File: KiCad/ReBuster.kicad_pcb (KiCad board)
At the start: 4 copper layers, 38 x 38 mm, 37 parts, among them U1 10M02SCU169, U2 LM1117-3.3, U3 SN74CBTD16210, U4 SN74LVC16T245DGVR, U5 SN74CBTD16210, U6 SN74CBTD16210, U7 74LVC2T45DC, U8 PLCC_84_plug, U9 PLCC_84_plug

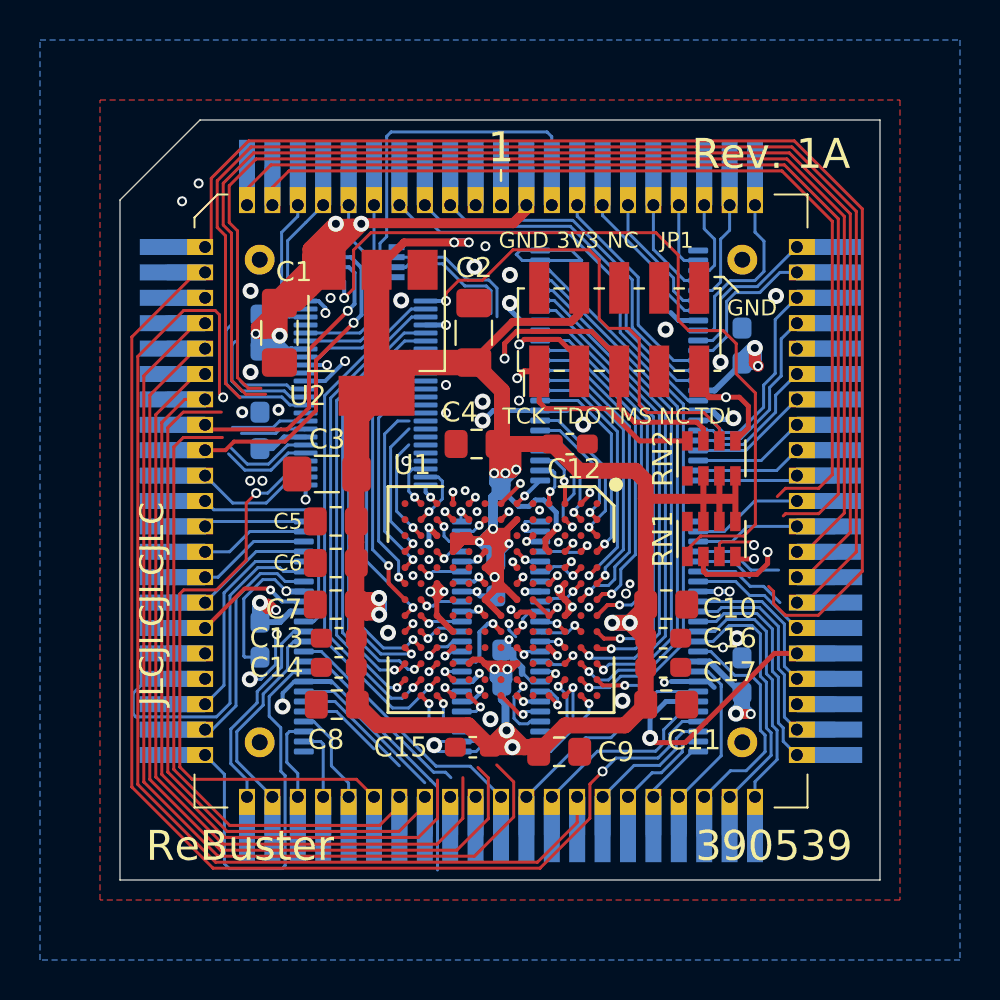
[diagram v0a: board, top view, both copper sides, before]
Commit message: Route EDS2 to U4 (SN74LVC16T245DGVR) change K13 -> K2 in FPGA
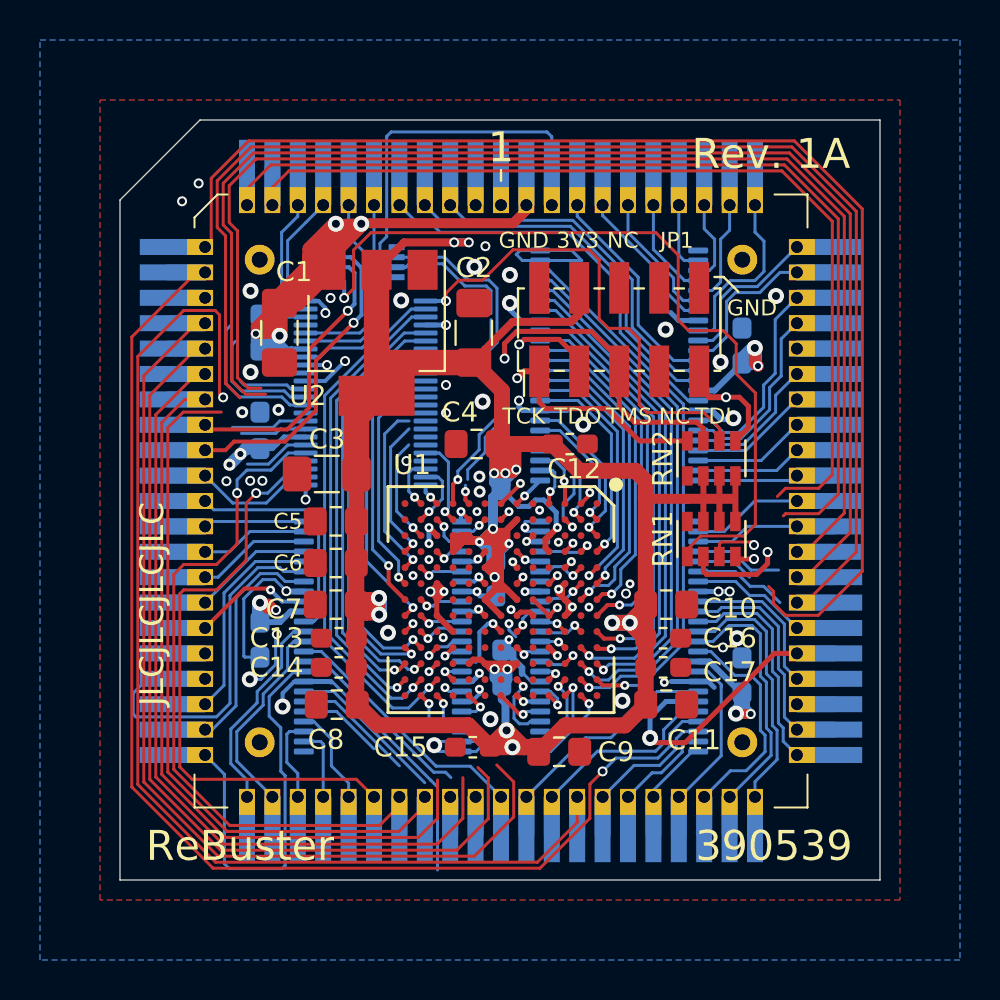
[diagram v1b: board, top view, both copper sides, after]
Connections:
- U1 pad K13: EDS2_FPGA -> Net-(U1-PadK13)
- U1 pad K2: DTACK_FPGA -> EDS2_FPGA
- U4 pad 44: Net-(U4-Pad44) -> EDS2_FPGA
- U4 pad 5: Net-(U4-Pad5) -> EDS2
- U6 pad 42: EDS2_FPGA -> Net-(U6-Pad42)
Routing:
- net Net-(U1-PadK1): track 0.58 -> 10.7 mm
- net DTACK_FPGA: track 7.66 -> 16.5 mm, vias 1 -> 0
- net Net-(U4-Pad5): track 4.54 -> 0.00 mm
- net EDS2_FPGA: track 1.49 -> 4.44 mm
- net EDS2: track 33.9 -> 35.9 mm, vias 0 -> 2
- net VCC: track 75.8 -> 77.6 mm, vias 10 -> 12
- net GND: track 77.3 -> 75.7 mm
- net Net-(U4-Pad6): track 4.51 -> 3.31 mm
- net Net-(U6-Pad42): track 0.00 -> 0.92 mm, vias 0 -> 1
- net Net-(U1-PadJ1): track 0.45 -> 0.99 mm

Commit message: Route EDS3 to U4 (SN74LVC16T245DGVR) change K12 -> M3 in FPGA
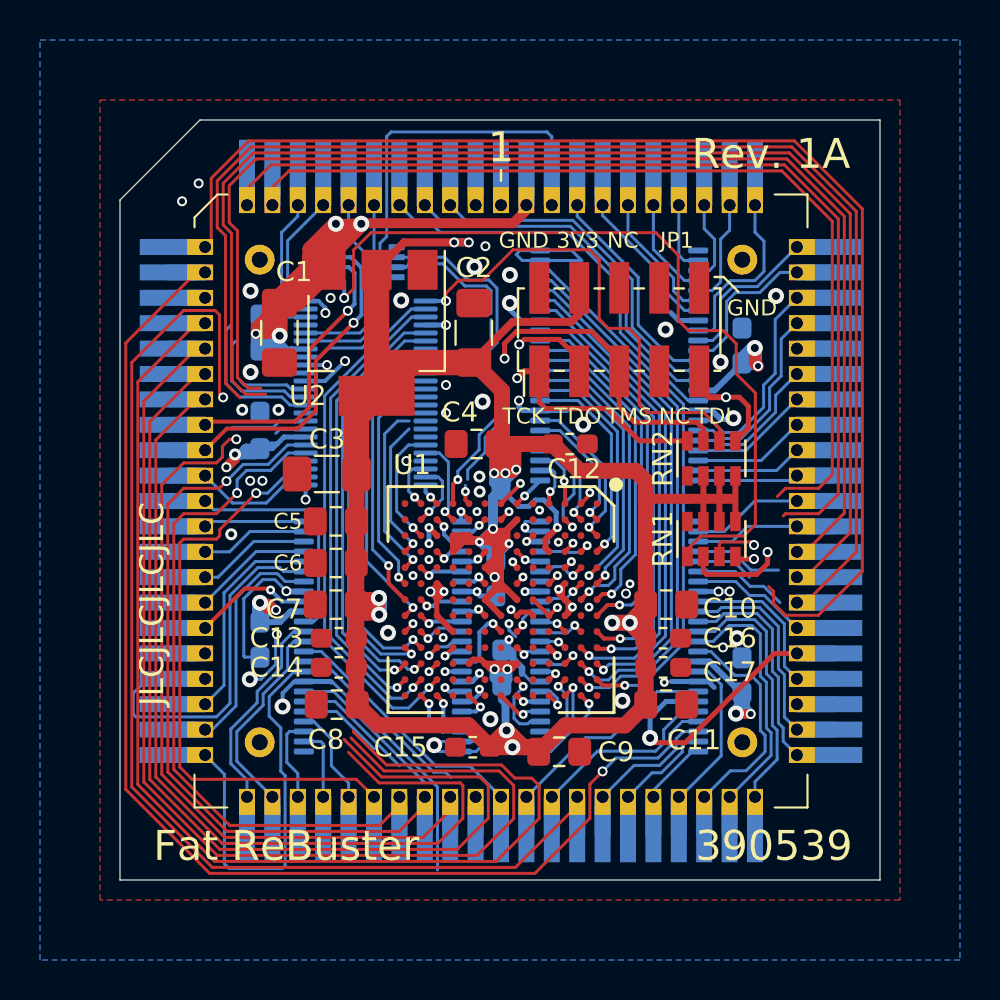
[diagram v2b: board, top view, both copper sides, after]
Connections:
- U1 pad K12: EDS3_FPGA -> Net-(U1-PadK12)
- U1 pad M3: SBR_FPGA -> EDS3_FPGA
- U4 pad 43: Net-(U4-Pad43) -> EDS3_FPGA
- U4 pad 6: Net-(U4-Pad6) -> EDS3
- U6 pad 40: EDS3_FPGA -> Net-(U6-Pad40)
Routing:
- net LOCK_EA1: track 1.87 -> 38.3 mm, vias 0 -> 1
- net RMC: track 50.1 -> 61.2 mm
- net SBR: track 46.6 -> 56.6 mm
- net SBG: track 42.6 -> 52.3 mm
- net CIIN: track 39.5 -> 47.3 mm
- net SBR_FPGA: track 5.30 -> 0.00 mm, vias 1 -> 0
- net EDS3_FPGA: track 1.41 -> 6.13 mm
- net Net-(U4-Pad6): track 3.31 -> 0.00 mm
- net VCC: track 77.6 -> 80.2 mm
- net Net-(U4-Pad8): track 3.37 -> 1.65 mm
- net EDS3: track 37.1 -> 38.4 mm, vias 0 -> 1
- net Net-(U6-Pad40): track 0.00 -> 0.84 mm, vias 0 -> 1
- net STERM: track 63.8 -> 64.5 mm
- net 3V3: track 204.4 -> 205.1 mm
- net EDS2: vias 2 -> 1
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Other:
- board text added: "Fat ReBuster"
- board text removed: "ReBuster"

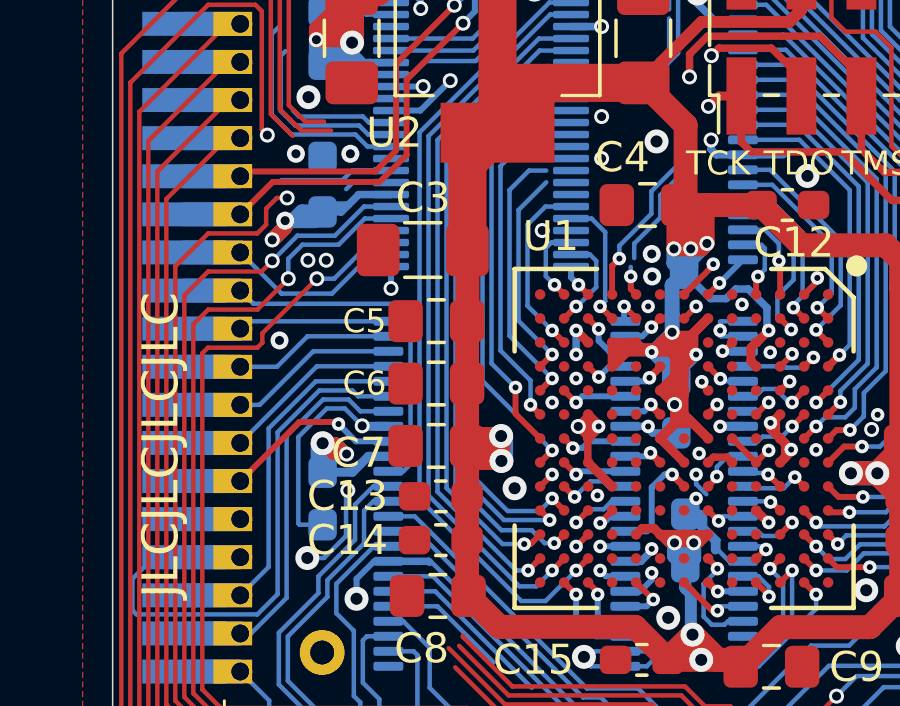
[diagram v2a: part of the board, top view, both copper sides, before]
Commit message: Route EA1_LOCK to U4 (SN74LVC16T245DGVR) change K10 -> N4 in FPGA
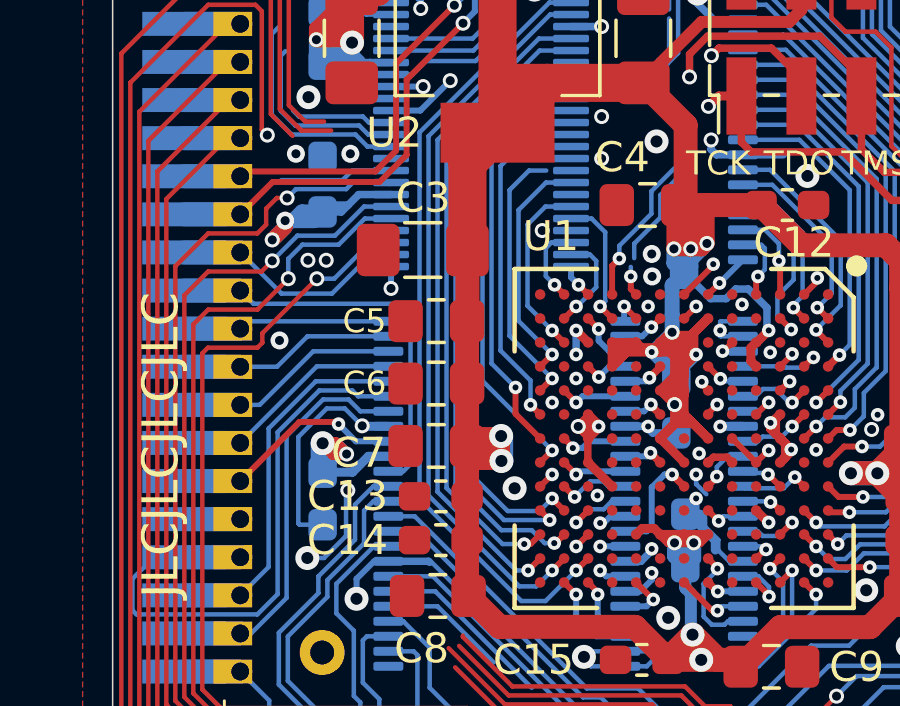
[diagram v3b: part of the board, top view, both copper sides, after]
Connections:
- U1 pad K10: LOCK_EA1_FPGA -> Net-(U1-PadK10)
- U1 pad N4: RMC_FPGA -> LOCK_EA1_FPGA
- U4 pad 41: Net-(U4-Pad41) -> LOCK_EA1_FPGA
- U4 pad 8: Net-(U4-Pad8) -> LOCK_EA1
- U6 pad 38: LOCK_EA1_FPGA -> Net-(U6-Pad38)
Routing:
- net RMC_FPGA: track 7.15 -> 0.00 mm, vias 1 -> 0
- net LOCK_EA1_FPGA: track 1.52 -> 7.97 mm
- net LOCK_EA1: track 38.3 -> 42.0 mm
- net Net-(U4-Pad8): track 1.65 -> 0.00 mm
- net Net-(U6-Pad38): track 0.00 -> 0.93 mm, vias 0 -> 1

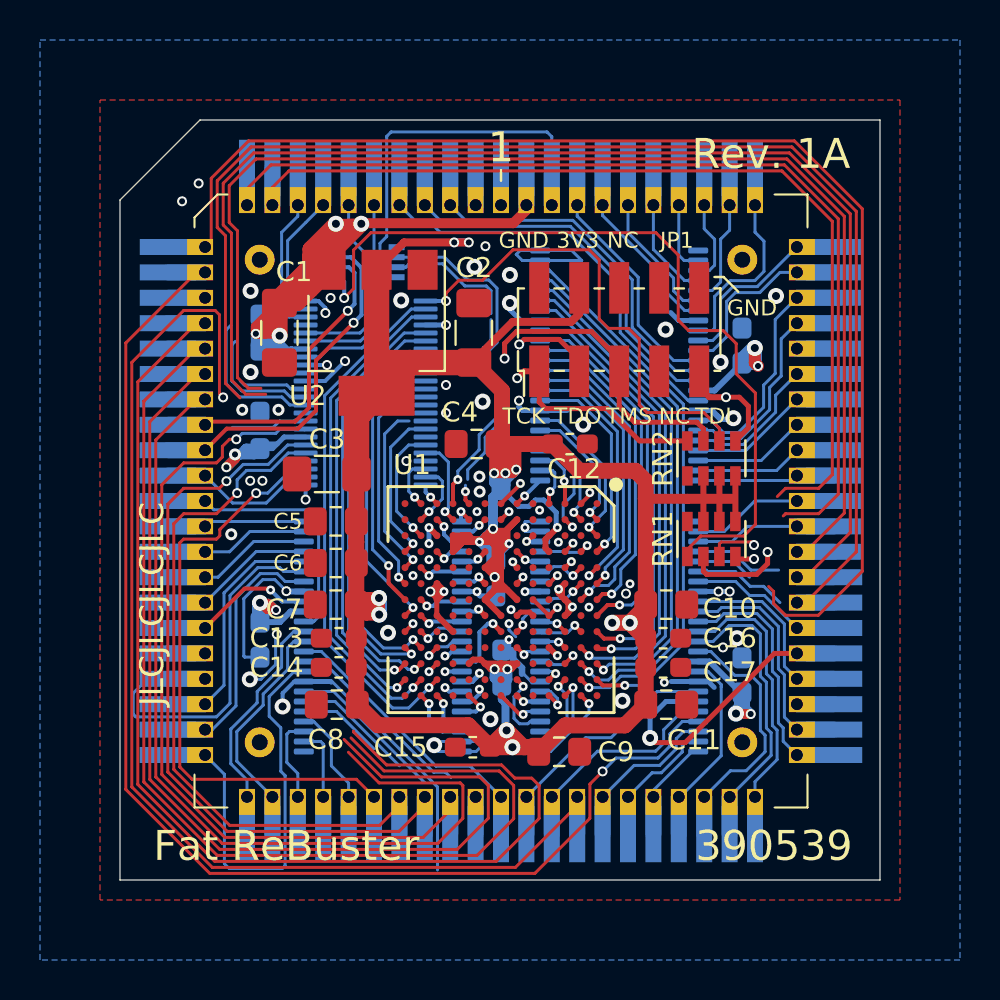
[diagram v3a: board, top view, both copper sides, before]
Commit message: Route MTCR to U4 (SN74LVC16T245DGVR) change F12 -> N5 in FPGA
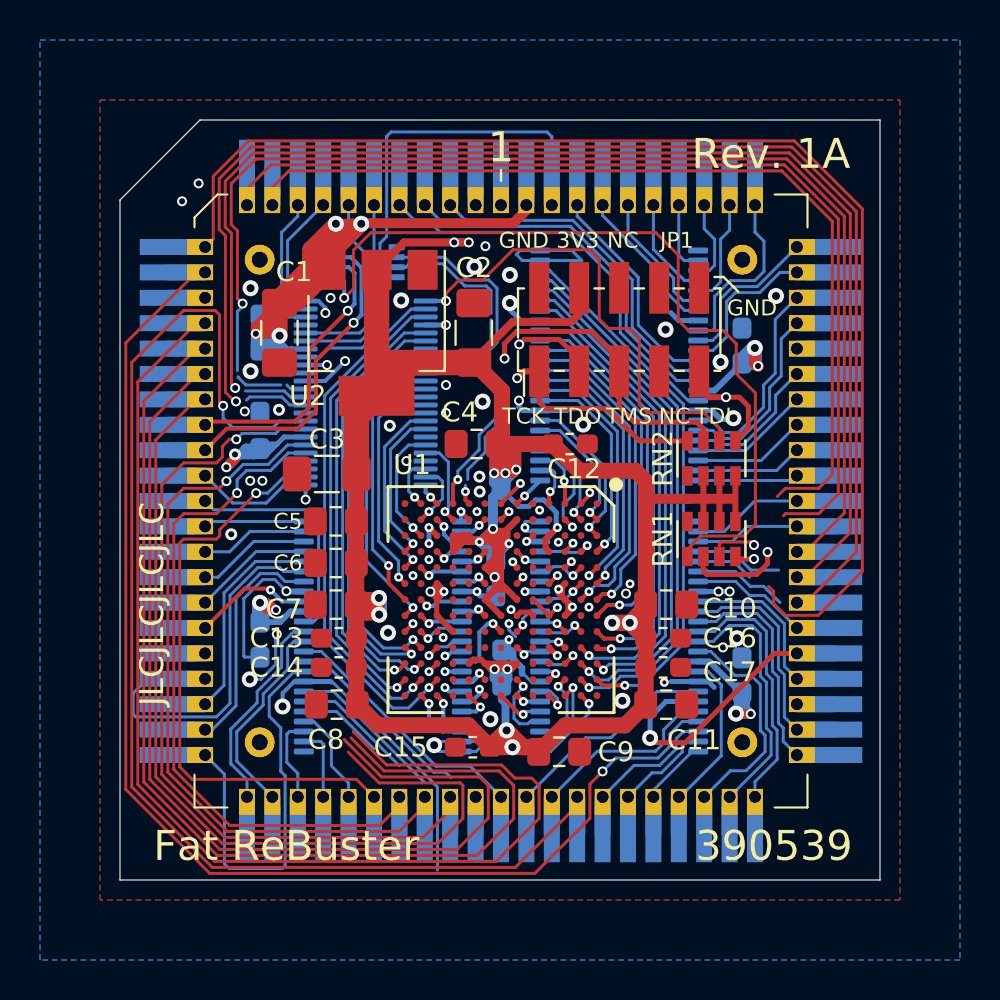
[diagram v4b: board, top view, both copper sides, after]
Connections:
- U1 pad N5: Net-(U1-PadN5) -> MTCR_FPGA
- U4 pad 40: Net-(U4-Pad40) -> MTCR_FPGA
- U4 pad 9: Net-(U4-Pad9) -> MTCR
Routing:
- net MTCR_FPGA: track 0.00 -> 9.38 mm, vias 0 -> 1
- net Net-(U1-PadN5): track 8.93 -> 0.00 mm, vias 1 -> 0
- net MTCR: track 58.5 -> 64.0 mm
- net Net-(U4-Pad11): track 7.43 -> 3.19 mm
- net Net-(U4-Pad9): track 3.79 -> 0.00 mm
- net Net-(U4-Pad12): track 6.06 -> 3.14 mm
- net Net-(U4-Pad13): track 3.43 -> 1.02 mm
- net EDS0: track 63.5 -> 61.8 mm, vias 0 -> 1
- net VCC: track 80.2 -> 81.0 mm
- net EA3: track 66.7 -> 67.4 mm, vias 0 -> 1
- net EA2: track 68.2 -> 68.3 mm, vias 0 -> 1
- net GND: vias 57 -> 58

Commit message: Route EA2,EA3 to U4 (SN74LVC16T245DGVR) change D6 -> N6, B5 -> N7 in FPGA
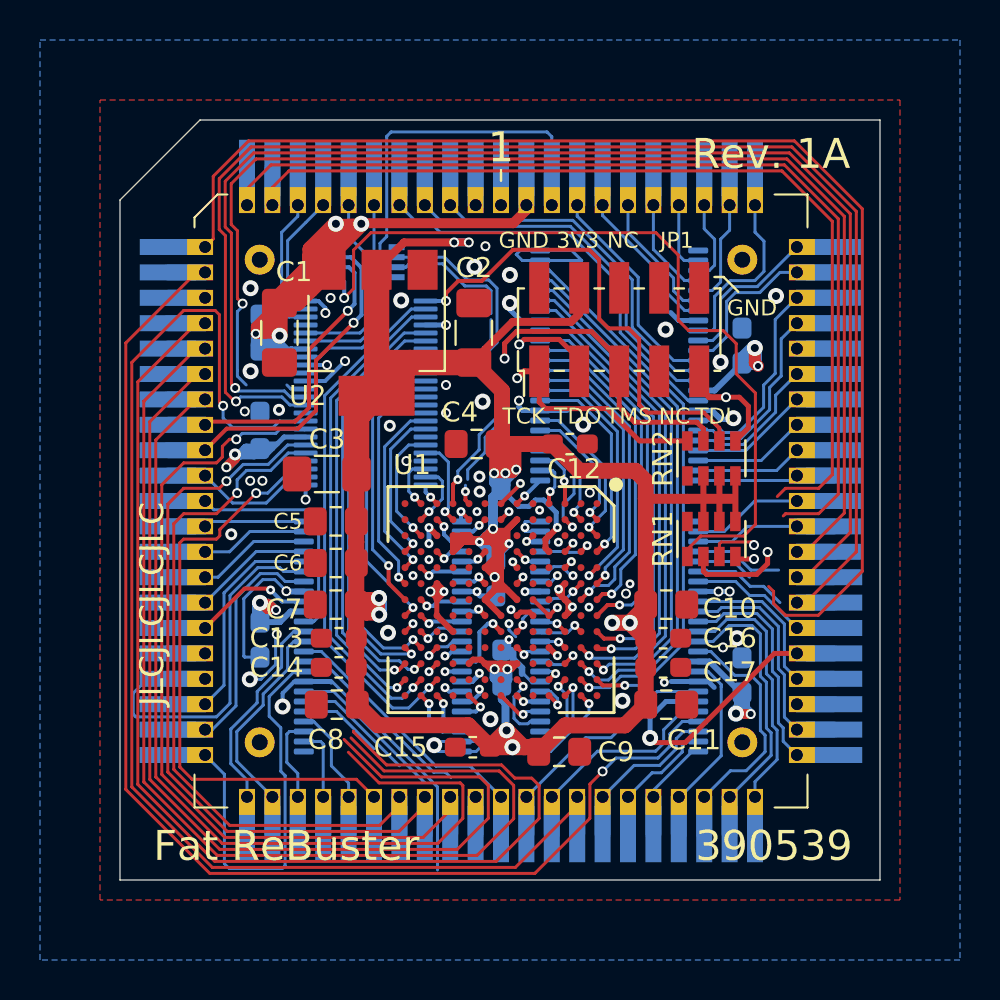
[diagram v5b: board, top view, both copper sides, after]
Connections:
- U1 pad B5: EA3_FPGA -> Net-(U1-PadB5)
- U1 pad D6: EA2_FPGA -> Net-(U1-PadD6)
- U1 pad N6: Net-(U1-PadN6) -> EA2_FPGA
- U1 pad N7: Net-(U1-PadN7) -> EA3_FPGA
- U4 pad 11: Net-(U4-Pad11) -> EA2
- U4 pad 12: Net-(U4-Pad12) -> EA3
- U4 pad 37: Net-(U4-Pad37) -> EA3_FPGA
- U4 pad 38: Net-(U4-Pad38) -> EA2_FPGA
- U5 pad 42: EA2_FPGA -> Net-(U5-Pad42)
- U5 pad 43: EA3_FPGA -> Net-(U5-Pad43)
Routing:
- net Net-(U1-PadN7): track 12.1 -> 0.00 mm, vias 1 -> 0
- net Net-(U1-PadN6): track 10.6 -> 0.00 mm, vias 1 -> 0
- net EA3_FPGA: track 2.49 -> 12.9 mm
- net EA2_FPGA: track 1.57 -> 11.4 mm
- net JP1: track 5.64 -> 0.00 mm, vias 1 -> 0
- net EA2: track 68.3 -> 72.0 mm
- net Net-(U4-Pad11): track 3.19 -> 0.00 mm, vias 1 -> 0
- net Net-(U4-Pad12): track 3.14 -> 0.00 mm, vias 1 -> 0
- net Net-(U5-Pad43): track 0.00 -> 1.93 mm, vias 0 -> 1
- net EA3: track 67.4 -> 68.8 mm
- net Net-(U5-Pad42): track 0.00 -> 0.98 mm, vias 0 -> 1
- net EDS0: track 61.8 -> 62.7 mm
- net OE_U4: track 34.7 -> 35.3 mm
- net GND: vias 58 -> 59
